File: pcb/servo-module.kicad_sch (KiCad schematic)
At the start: 20 parts, among them J1 AVR-UPDI-6, J2 QWICC, J3 Power, U2 ATtiny1616-M

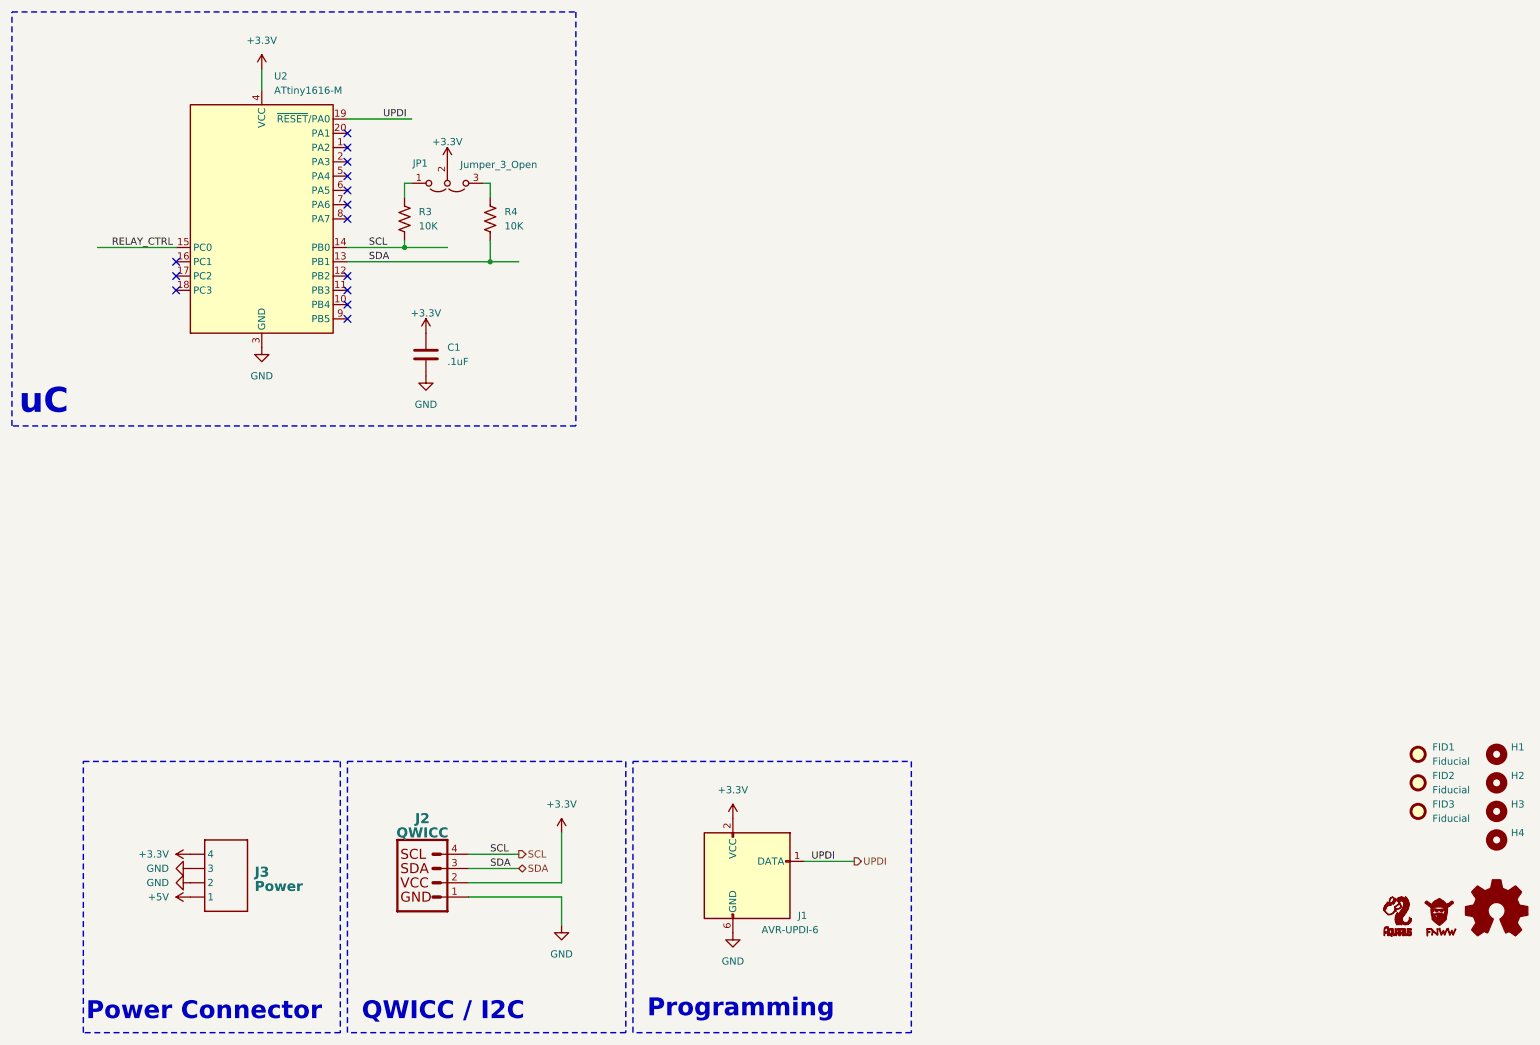
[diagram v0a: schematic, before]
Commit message: added connectors
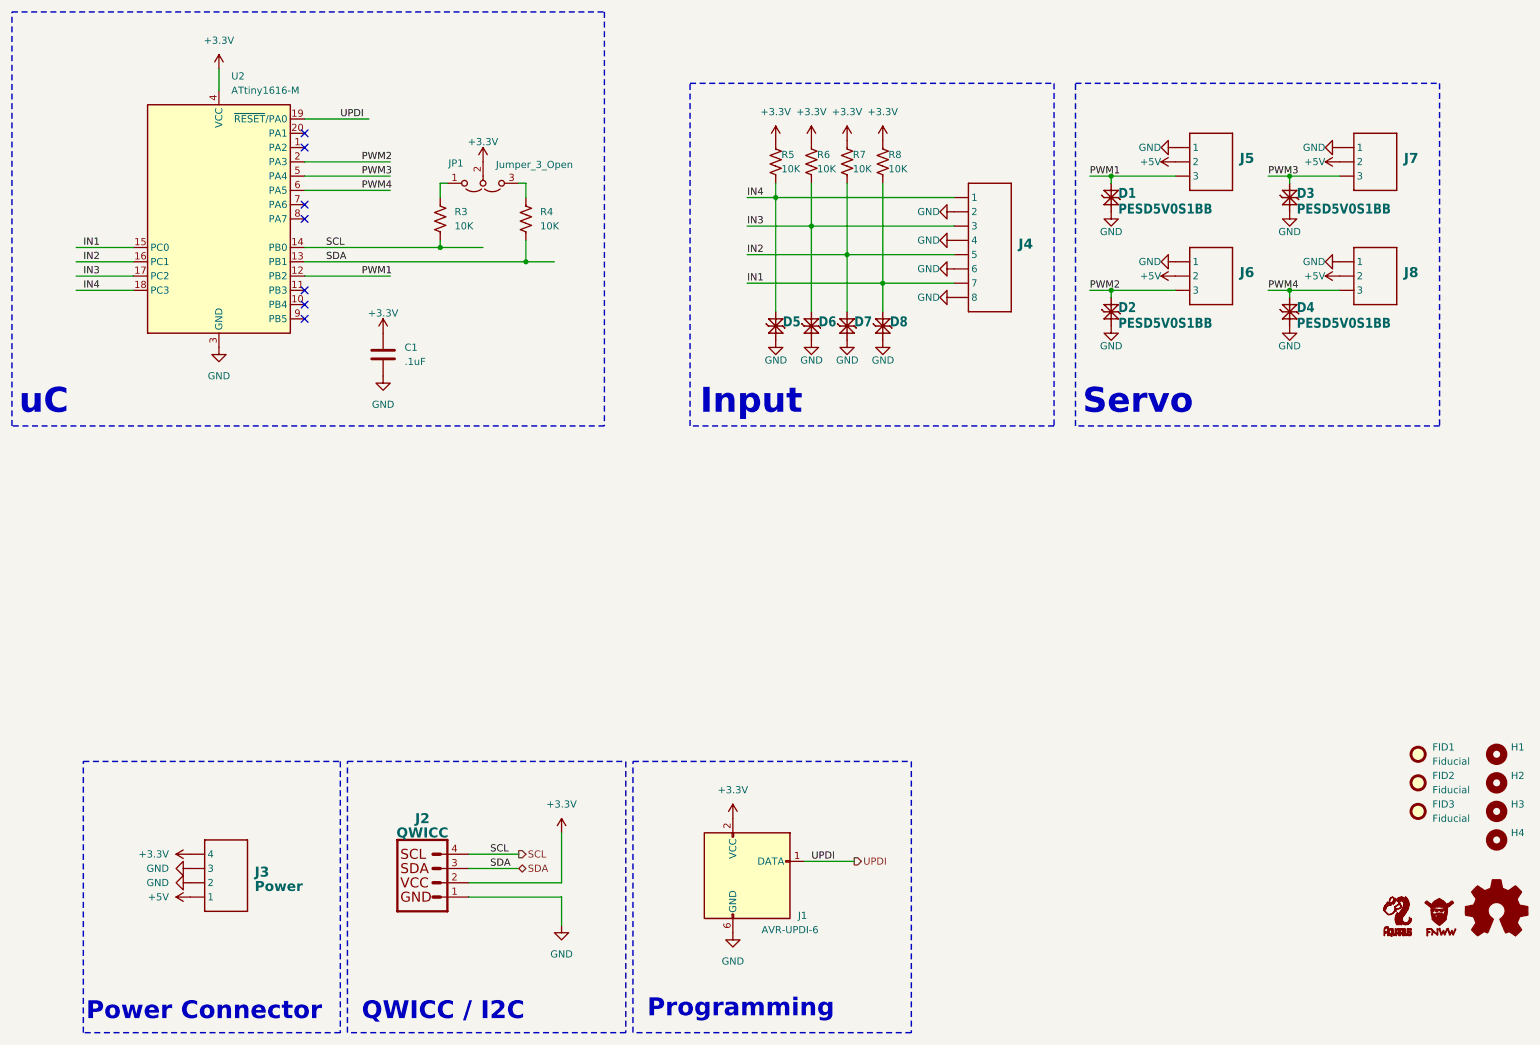
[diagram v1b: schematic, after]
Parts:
- added D1, D2, D3, D4, D5, D6, D7, D8: PESD5V0S1BB, CRGM Passive:D_SOD-523, symbol CRGM Passive:PESD5V0S1BB
- added J4: ~, Connector_JST:JST_SH_BM08B-SRSS-TB_1x08-1MP_P1.00mm_Vertical, symbol CRGM Connector:JST-SH-8
- added J5, J6, J7, J8: ~, Connector_JST:JST_SH_BM03B-SRSS-TB_1x03-1MP_P1.00mm_Vertical, symbol CRGM Connector:JST-SH-3
- added R5, R6, R7, R8: 10K, Resistor_SMD:R_0603_1608Metric, symbol Device:R_US
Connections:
- net +3.3V: now also R5.2, R6.2, R7.2, R8.2
- net +5V: now also J5.2, J6.2, J7.2, J8.2
- net GND: now also D1.1 (K1), D2.1 (K1), D3.1 (K1), D4.1 (K1), D5.1 (K1), D6.1 (K1), D7.1 (K1), D8.1 (K1), J4.2, J4.4, J4.6, J4.8, J5.1, J6.1, J7.1, J8.1
- net PWM1: now reaches U2.12 (PB2)
- net PWM1: now also D1.2 (K2), J5.3
- net IN2: now reaches U2.16 (PC1)
- net IN2: now also D7.2 (K2), J4.5, R7.1
- net IN3: now reaches U2.17 (PC2)
- net IN3: now also D6.2 (K2), J4.3, R6.1
- net IN4: now reaches U2.18 (PC3)
- net IN4: now also D5.2 (K2), J4.1, R5.1
- net PWM2: now reaches U2.2 (PA3)
- net PWM2: now also D2.2 (K2), J6.3
- net PWM3: now reaches U2.5 (PA4)
- net PWM3: now also D3.2 (K2), J7.3
- net PWM4: now reaches U2.6 (PA5)
- net PWM4: now also D4.2 (K2), J8.3
- net RELAY_CTRL renamed IN1
- net IN1: now also D8.2 (K2), J4.7, R8.1
- no-connect marks 14 -> 7
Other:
- note added: "Input"
- note added: "Servo"
- moved on the sheet: C1, JP1, R3, R4, U2

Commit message: Added additional suppliers and changed some footprints for DRC
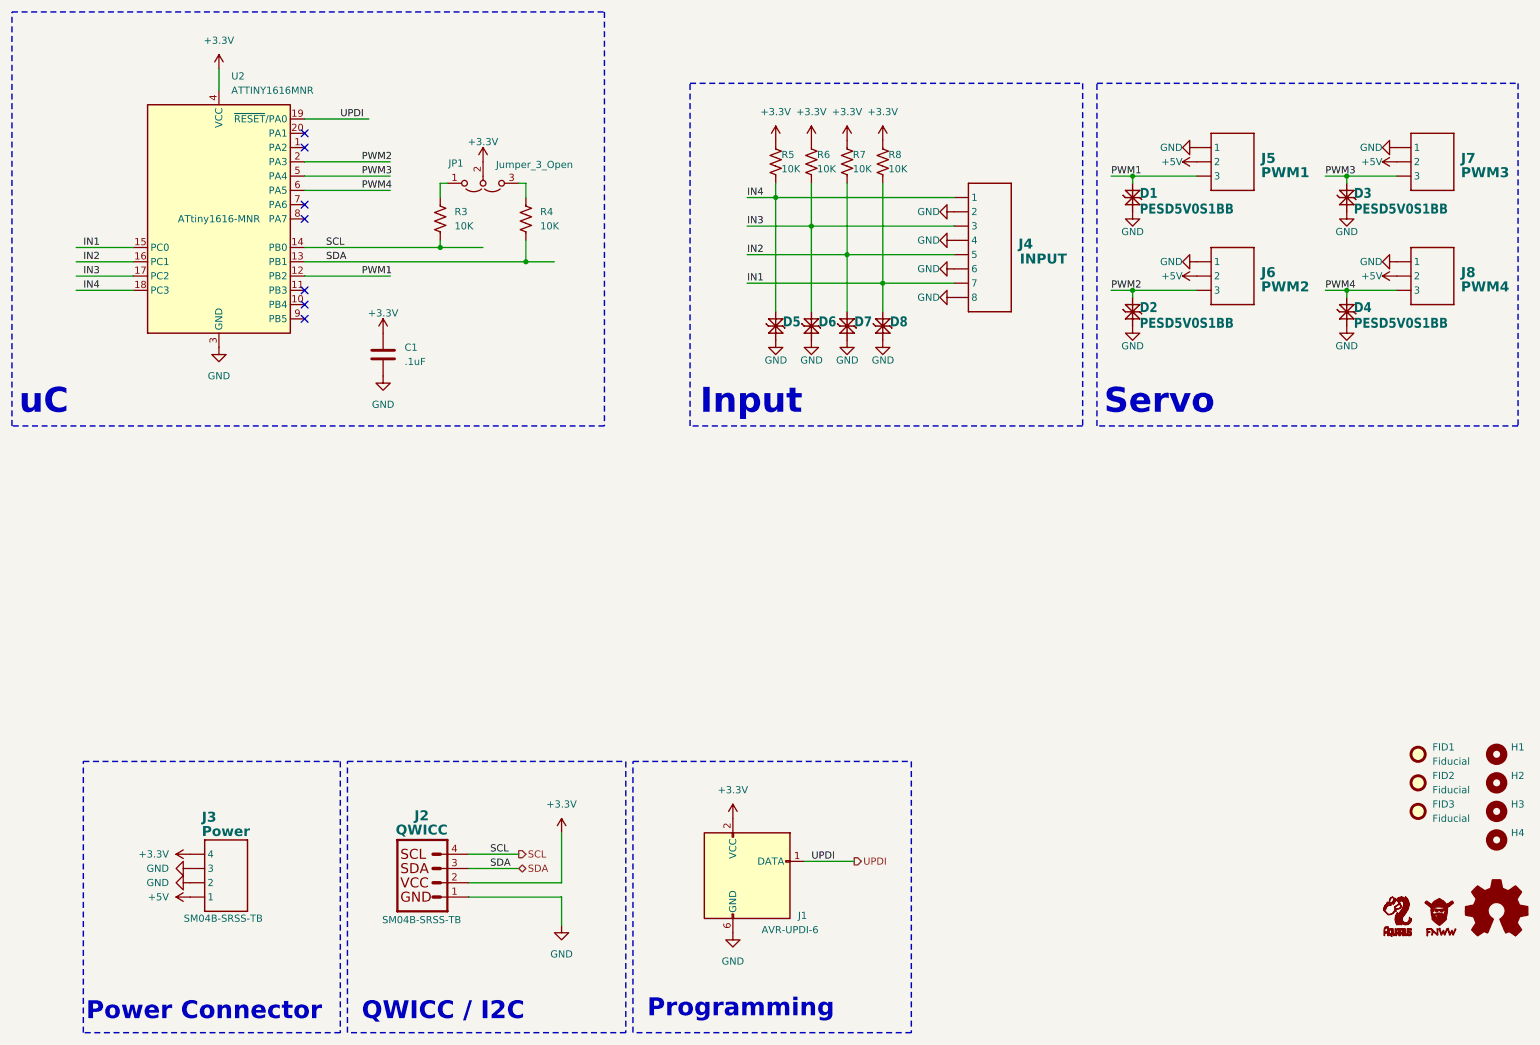
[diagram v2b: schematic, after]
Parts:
- J2: Digikey (none) -> 455-SM04B-SRSS-TBTR-ND; LCSC (none) -> C2763614; LCSC_PN C2763614 -> (none); MN (none) -> JST; MPN (none) -> SM04B-SRSS-TB; Mouser (none) -> 306-SM04BSRSSTBLFSN
- J3: Digikey (none) -> 455-SM04B-SRSS-TBTR-ND; Mouser (none) -> 306-SM04BSRSSTBLFSN
- J4: value ~ -> INPUT; Digikey (none) -> 455-BM08B-SRSS-TBTR-ND; LCSC (none) -> C2845376; Mouser (none) -> 306-BM08BSRSSTBLFSN
- J5: value ~ -> PWM1; Digikey (none) -> 455-BM03B-SRSS-TBTR-ND; LCSC (none) -> C2763613; MN (none) -> JST; MPN (none) -> BM03B-SRSS-TB; Mouser (none) -> 306-BM03BSRSSTBLFSNP
- J6: value ~ -> PWM2; Digikey (none) -> 455-BM03B-SRSS-TBTR-ND; LCSC (none) -> C2763613; MN (none) -> JST; MPN (none) -> BM03B-SRSS-TB; Mouser (none) -> 306-BM03BSRSSTBLFSNP
- J7: value ~ -> PWM3; Digikey (none) -> 455-BM03B-SRSS-TBTR-ND; LCSC (none) -> C2763613; MN (none) -> JST; MPN (none) -> BM03B-SRSS-TB; Mouser (none) -> 306-BM03BSRSSTBLFSNP
- J8: value ~ -> PWM4; Digikey (none) -> 455-BM03B-SRSS-TBTR-ND; LCSC (none) -> C2763613; MN (none) -> JST; MPN (none) -> BM03B-SRSS-TB; Mouser (none) -> 306-BM03BSRSSTBLFSNP
- U2: value ATtiny1616-M -> ATTINY1616MNR; Digilkey (none) -> ATTINY1616-MNRTR-ND; LCSC (none) -> C507118; LCSC_PN C507118 -> (none); MN (none) -> Atmel; MPN (none) -> ATtiny1616-MNR; Mouser (none) -> 556-ATTINY1616MNR
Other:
- moved on the sheet: D1, D2, D3, D4, J5

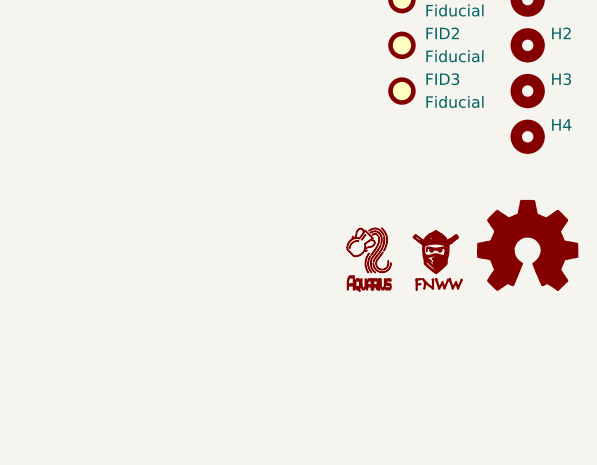
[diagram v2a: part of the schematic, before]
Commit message: Updated silkscreen
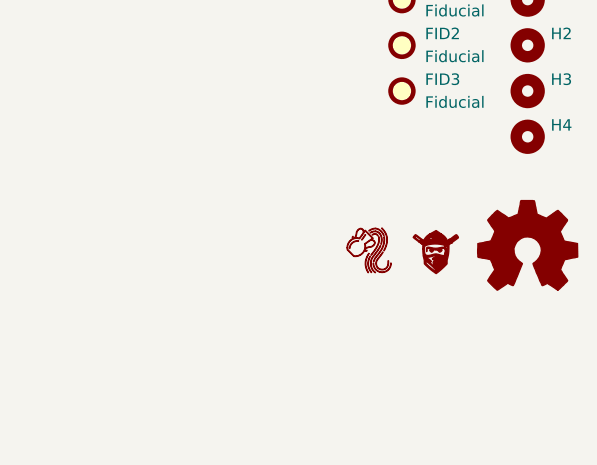
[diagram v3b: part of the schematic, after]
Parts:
- removed LOGO2: ~, CRGM Logos:Aquarius Name 2mmx5mm, symbol CRGM Logos:Aquarius Name
- removed LOGO4: ~, CRGM Logos:FNWW Name 2mmx5mm, symbol CRGM Logos:FNWW Name
- LOGO1: footprint CRGM Logos:Aquarius Logo 5mm -> CRGM Logos:Aquarius Logo 10mm
- LOGO3: footprint CRGM Logos:FNWW Face 5mm -> CRGM Logos:FNWW Face 10mm
- LOGO5: footprint Symbol:OSHW-Symbol_6.7x6mm_SilkScreen -> Symbol:OSHW-Logo_5.7x6mm_SilkScreen
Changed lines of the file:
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@@
 			)
 		)
-		(property "Footprint" "CRGM Logos:Aquarius Logo 5mm"
+		(property "Footprint" "CRGM Logos:Aquarius Logo 10mm"
 			(at 261.874 179.578 0)
 			(effects
@@
 			)
 		)
-		(property "Footprint" "Symbol:OSHW-Symbol_6.7x6mm_SilkScreen"
+		(property "Footprint" "Symbol:OSHW-Logo_5.7x6mm_SilkScreen"
 			(at 278.13 173.99 0)
 			(effects
@@
 	)
 	(symbol
-		(lib_id "CRGM Logos:Aquarius Name")
-		(at 260.3903 178.523 0)
-		(unit 1)
-		(exclude_from_sim no)
-		(in_bom no)
-		(on_board yes)
-		(dnp no)
-		(fields_autoplaced yes)
-		(property "Reference" "LOGO2"
-			(at 260.1363 179.539 0)
-			(effects
-				(font
-					(size 1.27 1.27)
-				)
-				(hide yes)
-			)
-		)
-		(property "Value" "~"
-			(at 258.1043 176.745 0)
-			(effects
-				(font
-					(size 1.27 1.27)
-				)
-				(hide yes)
-			)
-		)
-		(property "Footprint" "CRGM Logos:Aquarius Name 2mmx5mm"
-			(at 261.4063 181.063 0)
-			(effects
-				(font
-					(size 1.27 1.27)
-				)
-				(hide yes)
-			)
-		)
-		(property "Datasheet" ""
-			(at 258.1043 176.745 0)
-			(effects
-				(font
-					(size 1.27 1.27)
-				)
-				(hide yes)
-			)
-		)
-		(property "Description" ""
-			(at 258.1043 176.745 0)
-			(effects
-				(font
-					(size 1.27 1.27)
-				)
-				(hide yes)
-			)
-		)
-		(property "MPN" ""
-			(at 260.3903 178.523 0)
-			(effects
-				(font
-					(size 1.27 1.27)
-				)
-			)
-		)
-		(instances
-			(project ""
-				(path "/445c1fff-2e1a-48b1-a91f-a137832edebf"
-					(reference "LOGO2")
-					(unit 1)
-				)
-			)
-		)
-	)
-	(symbol
 		(lib_id "CRGM Passive:PESD5V0S1BB")
 		(at 149.86 69.85 90)
@@
 	)
 	(symbol
-		(lib_id "CRGM Logos:FNWW Name")
-		(at 267.97 177.8 0)
-		(unit 1)
-		(exclude_from_sim no)
-		(in_bom no)
-		(on_board yes)
-		(dnp no)
-		(fields_autoplaced yes)
-		(property "Reference" "LOGO4"
-			(at 268.224 179.578 0)
-			(effects
-				(font
-					(size 1.27 1.27)
-				)
-				(hide yes)
-			)
-		)
-		(property "Value" "~"
-			(at 267.991 183.4101 0)
-			(effects
-				(font
-					(size 1.27 1.27)
-				)
-				(hide yes)
-			)
-		)
-		(property "Footprint" "CRGM Logos:FNWW Name 2mmx5mm"
-			(at 271.526 182.118 0)
-			(effects
-				(font
-					(size 1.27 1.27)
-				)
-				(hide yes)
-			)
-		)
-		(property "Datasheet" ""
-			(at 267.991 183.4101 0)
-			(effects
-				(font
-					(size 1.27 1.27)
-				)
-				(hide yes)
-			)
-		)
-		(property "Description" ""
-			(at 267.991 183.4101 0)
-			(effects
-				(font
-					(size 1.27 1.27)
-				)
-				(hide yes)
-			)
-		)
-		(property "MPN" ""
-			(at 267.97 177.8 0)
-			(effects
-				(font
-					(size 1.27 1.27)
-				)
-			)
-		)
-		(instances
-			(project ""
-				(path "/445c1fff-2e1a-48b1-a91f-a137832edebf"
-					(reference "LOGO4")
-					(unit 1)
-				)
-			)
-		)
-	)
-	(symbol
 		(lib_id "power:+3.3V")
 		(at 97.79 40.64 0)
@@
 			)
 		)
-		(property "Footprint" "CRGM Logos:FNWW Face 5mm"
+		(property "Footprint" "CRGM Logos:FNWW Face 10mm"
 			(at 267.97 179.578 0)
 			(effects
